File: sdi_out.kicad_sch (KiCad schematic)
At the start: 21 parts, among them U1 GS2988-INE3

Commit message: implement schematic review feedback
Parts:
- added C81: 100n, Capacitor_SMD:C_0402_1005Metric, symbol Device:C
- added R71, R75: 49.9, Resistor_SMD:R_0402_1005Metric, symbol Device:R
- added R79: 10k, Resistor_SMD:R_0603_1608Metric, symbol Device:R
- C18: renamed from C16; footprint Capacitor_SMD:C_0402_1005Metric -> Capacitor_SMD:C_0603_1608Metric
- C19: renamed from C17; footprint Capacitor_SMD:C_0402_1005Metric -> Capacitor_SMD:C_0603_1608Metric
- C20: renamed from C18; footprint Capacitor_SMD:C_0402_1005Metric -> Capacitor_SMD:C_0603_1608Metric
- C24: renamed from C19; footprint Capacitor_SMD:C_0402_1005Metric -> Capacitor_SMD:C_0603_1608Metric
- renumbered C4 to C16, C5 to C17, C20 to C22, C3 to C23, D1 to D3, L2 to L3, R1 to R17, R2 to R18, R58 to R19, R59 to R20, R11 to R21, R7 to R22, R8 to R23, R9 to R24, RF2 to RF3, U1 to U3
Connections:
- net GND: now also C81.2
- net ~{DISABLE}: now also R79.2
- net at C18.2, U3.1 (DDI): now also R71.1
- net at C19.2, U3.2 (~{DDI}): now also R75.2
- new net: C81.1, R71.2, R75.1
- new net VIO_GOOD: R79.1
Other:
- note added: "Input Termination for LMH0302 compatibility."
- moved on the sheet: C16, C17, C18, C19, R17

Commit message: substitute bnc connector for better max freq
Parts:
- removed RF3: DOSIN-801-0057, JLCImport:DOSIN-801-0057, symbol JLCImport:DOSIN-801-0057
- added J3: Conn_Coaxial, JLCImport:CONN_73171-1900_MOL, symbol Connector:Conn_Coaxial
- renumbered C16 to C20, C17 to C21, C18 to C22, C19 to C23, C81 to C24, C20 to C25, C21 to C26, C22 to C27, C23 to C28, C24 to C29, R71 to R19, R75 to R20, R18 to R21, R17 to R22, R19 to R23, R20 to R24, R21 to R25, R22 to R26, R79 to R27, R23 to R28, R24 to R29
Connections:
- net GND: now also J3.2 (Ext)
- net at C29.2: now also J3.1 (In)

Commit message: split gpio expanders by inputs/outputs instead of quads
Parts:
- C42: renamed from C20; KiLib_Generator (none) -> SMD_2terminal_chip_molded
- C43: renamed from C21; KiLib_Generator (none) -> SMD_2terminal_chip_molded
- C44: renamed from C22; KiLib_Generator (none) -> SMD_2terminal_chip_molded
- C45: renamed from C23; KiLib_Generator (none) -> SMD_2terminal_chip_molded
- C46: renamed from C24; KiLib_Generator (none) -> SMD_2terminal_chip_molded
- C47: renamed from C25; KiLib_Generator (none) -> SMD_2terminal_chip_molded
- C48: renamed from C26; KiLib_Generator (none) -> SMD_2terminal_chip_molded
- C49: renamed from C27; KiLib_Generator (none) -> SMD_2terminal_chip_molded
- C50: renamed from C28; KiLib_Generator (none) -> SMD_2terminal_chip_molded
- C51: renamed from C29; KiLib_Generator (none) -> SMD_2terminal_chip_molded
- D5: renamed from D3; KiLib_Generator (none) -> SMD_2terminal_chip_molded
- L5: renamed from L3; KiLib_Generator (none) -> SMD_2terminal_chip_molded
- R33: renamed from R19; KiLib_Generator (none) -> SMD_2terminal_chip_molded
- R34: renamed from R20; KiLib_Generator (none) -> SMD_2terminal_chip_molded
- R35: renamed from R21; KiLib_Generator (none) -> SMD_2terminal_chip_molded
- R36: renamed from R22; KiLib_Generator (none) -> SMD_2terminal_chip_molded
- R37: renamed from R23; KiLib_Generator (none) -> SMD_2terminal_chip_molded
- R38: renamed from R24; KiLib_Generator (none) -> SMD_2terminal_chip_molded
- R39: renamed from R25; KiLib_Generator (none) -> SMD_2terminal_chip_molded
- R40: renamed from R26; KiLib_Generator (none) -> SMD_2terminal_chip_molded
- R41: renamed from R27; KiLib_Generator (none) -> SMD_2terminal_chip_molded
- R42: renamed from R28; KiLib_Generator (none) -> SMD_2terminal_chip_molded
- R43: renamed from R29; KiLib_Generator (none) -> SMD_2terminal_chip_molded
- renumbered J3 to J5, U3 to U7

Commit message: start laying out channels
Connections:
- net DDI+: now reaches C44.2, R33.1, U7.1 (DDI)
- net DDI-: now reaches C45.2, R34.2, U7.2 (~{DDI})
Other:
- moved on the sheet: C48, C49, J5, R39, R42

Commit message: finish layout of first in and out channel
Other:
- moved on the sheet: C48, C49, R39, R42

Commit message: route the smartvio mcu and the gpio expanders
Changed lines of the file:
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@@
 	(wire
 		(pts
-			(xy 40.64 78.74) (xy 46.99 78.74)
+			(xy 24.13 78.74) (xy 46.99 78.74)
 		)
 		(stroke
@@
 	(wire
 		(pts
-			(xy 40.64 96.52) (xy 46.99 96.52)
+			(xy 24.13 96.52) (xy 46.99 96.52)
 		)
 		(stroke
@@
 	(hierarchical_label "IN+"
 		(shape input)
-		(at 40.64 78.74 180)
+		(at 24.13 78.74 180)
 		(effects
 			(font
@@
 	(hierarchical_label "IN-"
 		(shape input)
-		(at 40.64 96.52 180)
+		(at 24.13 96.52 180)
 		(effects
 			(font
@@
 			(pts
 				(xy 135.255 82.55) (xy 135.255 86.995) (xy 133.985 86.995) (xy 133.985 82.55)
+			)
+			(stroke
+				(width 0)
+				(type dash)
+			)
+			(fill
+				(type none)
+			)
+		)
+	)
+	(rule_area
+		(exclude_from_sim no)
+		(in_bom yes)
+		(on_board yes)
+		(dnp no)
+		(polyline
+			(pts
+				(xy 26.6342 76.2) (xy 26.67 98.425) (xy 27.94 98.425) (xy 27.9042 76.2)
 			)
 			(stroke
@@
 			(show_name no)
 			(do_not_autoplace no)
+			(effects
+				(font
+					(size 1.27 1.27)
+					(italic yes)
+				)
+			)
+		)
+	)
+	(netclass_flag ""
+		(length 2.54)
+		(shape round)
+		(at 27.2692 76.2 0)
+		(effects
+			(font
+				(size 1.27 1.27)
+			)
+			(justify left bottom)
+		)
+		(property "Netclass" "100 Ohm Diff"
+			(at 24.4752 71.628 0)
+			(show_name no)
+			(do_not_autoplace no)
+			(effects
+				(font
+					(size 1.27 1.27)
+				)
+				(justify left)
+			)
+		)
+		(property "Component Class" ""
+			(at -158.1508 11.43 0)
+			(show_name no)
+			(do_not_autoplace no)

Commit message: finish routing
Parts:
- J5: Manufacturer (none) -> Molex; Manufacturer Part (none) -> 731711900
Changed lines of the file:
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@@
 			)
 		)
-		(property "Datasheet" ""
+		(property "Datasheet" "https://www.molex.com/en-us/products/part-detail/731711900?display=pdf"
 			(at 212.09 85.09 0)
 			(hide yes)
@@
 			(at 212.09 85.09 0)
 			(hide yes)
+			(show_name no)
+			(do_not_autoplace no)
+			(effects
+				(font
+					(size 1.27 1.27)
+				)
+			)
+		)
+		(property "Manufacturer" "Molex"
+			(at 212.09 85.09 0)
+			(hide yes)
+			(show_name no)
+			(do_not_autoplace no)
+			(effects
+				(font
+					(size 1.27 1.27)
+				)
+			)
+		)
+		(property "Manufacturer Part" "731711900"
+			(at 212.09 85.09 0)
+			(hide yes)

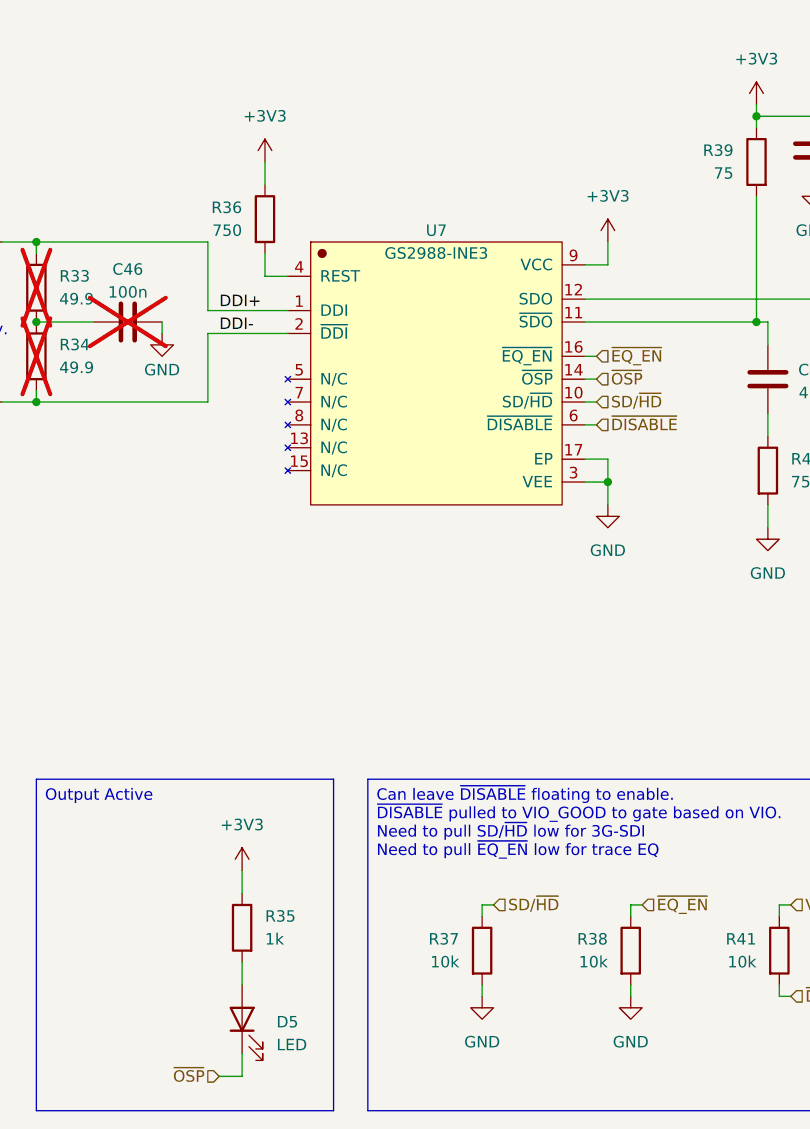
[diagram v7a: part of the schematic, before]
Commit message: fixes following review and more mounting holes
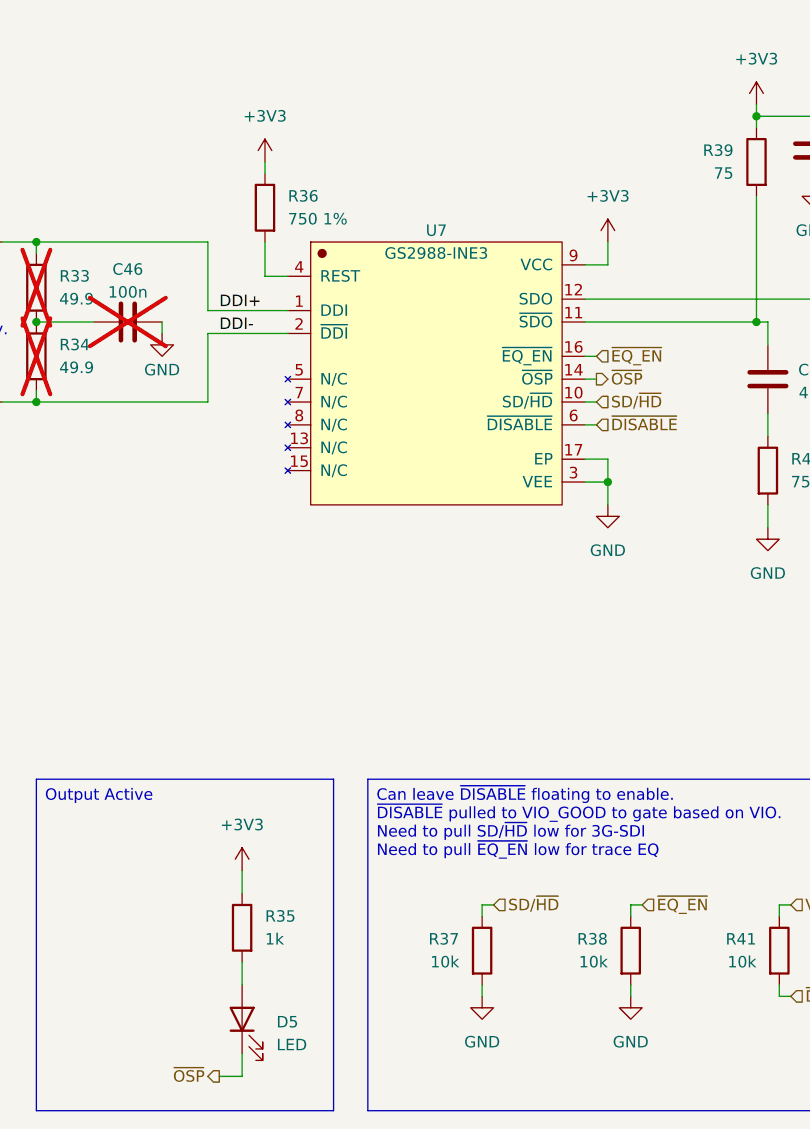
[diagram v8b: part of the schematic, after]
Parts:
- R36: value 750 -> 750 1%
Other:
- moved on the sheet: R36
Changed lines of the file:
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@@
 	(wire
 		(pts
-			(xy 83.82 69.85) (xy 83.82 72.39)
+			(xy 83.82 69.85) (xy 83.82 71.12)
 		)
 		(stroke
@@
 	(wire
 		(pts
-			(xy 83.82 80.01) (xy 83.82 82.55)
+			(xy 83.82 78.74) (xy 83.82 82.55)
 		)
 		(stroke
@@
 	)
 	(hierarchical_label "~{OSP}"
-		(shape input)
+		(shape output)
 		(at 120.65 93.98 0)
 		(effects
@@
 	)
 	(hierarchical_label "~{OSP}"
-		(shape input)
+		(shape output)
 		(at 78.74 171.45 180)
 		(effects
@@
 	(symbol
 		(lib_id "Device:R")
-		(at 83.82 76.2 0)
+		(at 83.82 74.93 0)
+		(mirror y)
 		(unit 1)
 		(body_style 1)
@@
 		(dnp no)
 		(property "Reference" "R36"
-			(at 81.28 74.9299 0)
+			(at 86.36 73.6599 0)
 			(show_name no)
 			(do_not_autoplace no)
@@
 			)
 		)
-		(property "Value" "750"
-			(at 81.28 77.4699 0)
+		(property "Value" "750 1%"
+			(at 86.36 76.1999 0)
 			(show_name no)
 			(do_not_autoplace no)
@@
 		)
 		(property "Footprint" "Resistor_SMD:R_0603_1608Metric"
-			(at 82.042 76.2 90)
+			(at 85.598 74.93 90)
 			(hide yes)
 			(show_name no)
@@
 		)
 		(property "Datasheet" ""
-			(at 83.82 76.2 0)
+			(at 83.82 74.93 0)
 			(hide yes)
 			(show_name no)
@@
 		)
 		(property "Description" "Resistor"
-			(at 83.82 76.2 0)
+			(at 83.82 74.93 0)
 			(hide yes)
 			(show_name no)
@@
 		)
 		(property "KiLib_Generator" "SMD_2terminal_chip_molded"
-			(at 83.82 76.2 0)
-			(hide yes)
-			(show_name no)
+			(at 83.82 74.93 0)
+			(hide yes)
+			(show_name no)
